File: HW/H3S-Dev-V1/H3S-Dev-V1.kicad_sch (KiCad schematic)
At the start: 20 parts, among them J1 USB_C_Receptacle_USB2.0_16P, J2 Conn_01x02_Socket, J3 Conn_Coaxial, Q1 DMP3099L, U1 Ai-Thinker-Ra-01, U2 LTC4054ES5-4.2, U3 USBLC6-2SC6, U4 ESP32-S3-WROOM-1

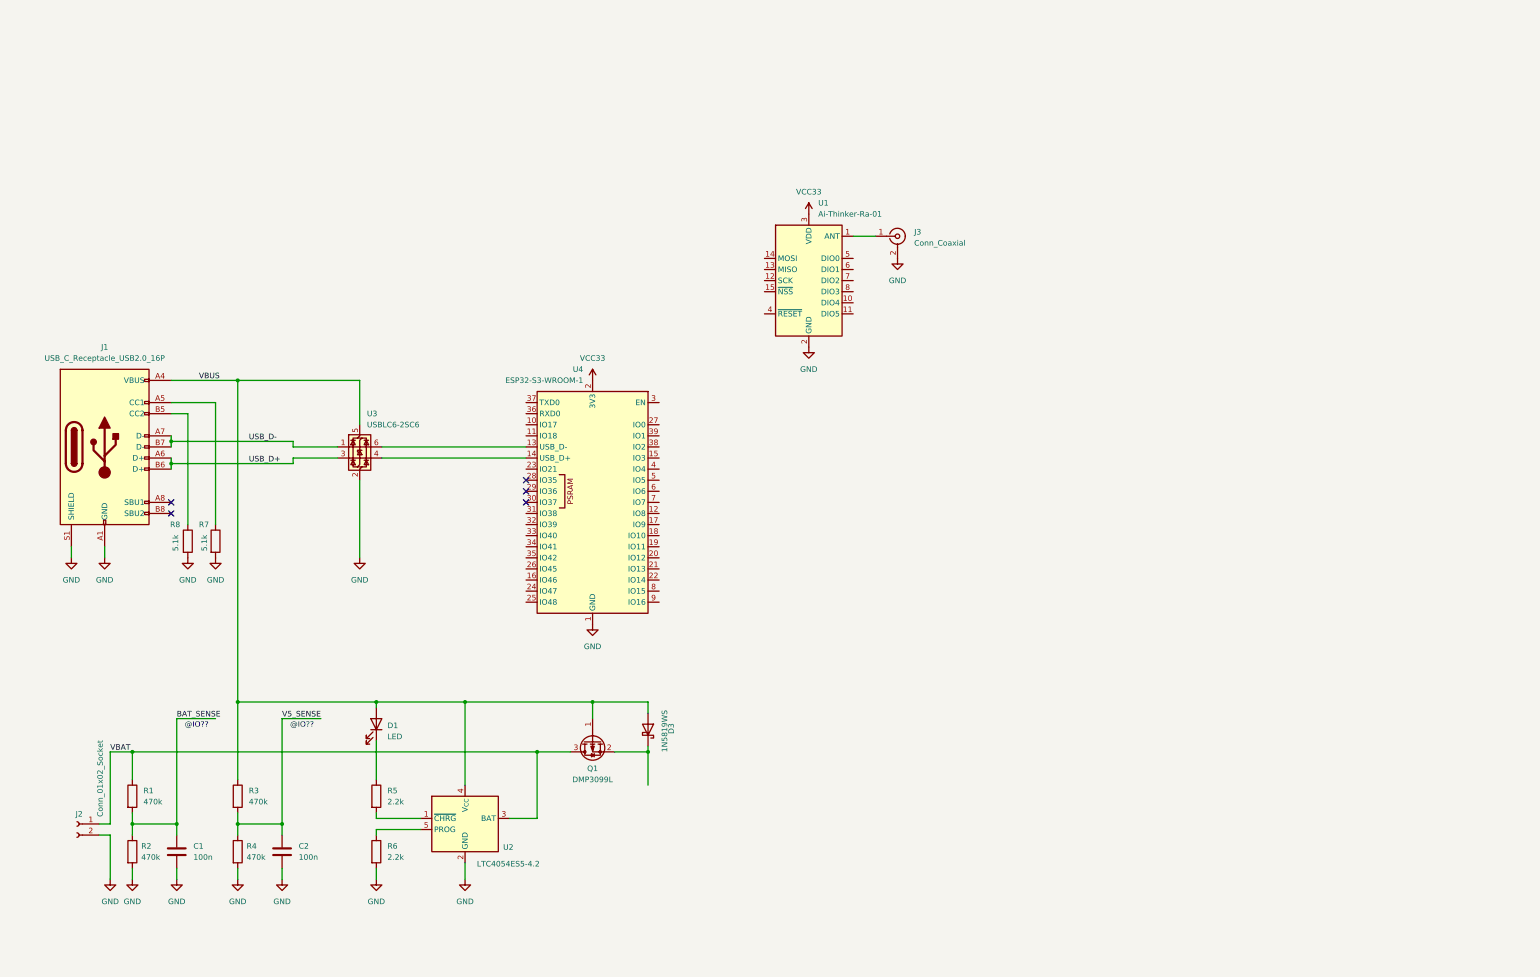
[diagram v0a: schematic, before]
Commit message: Some components arranged
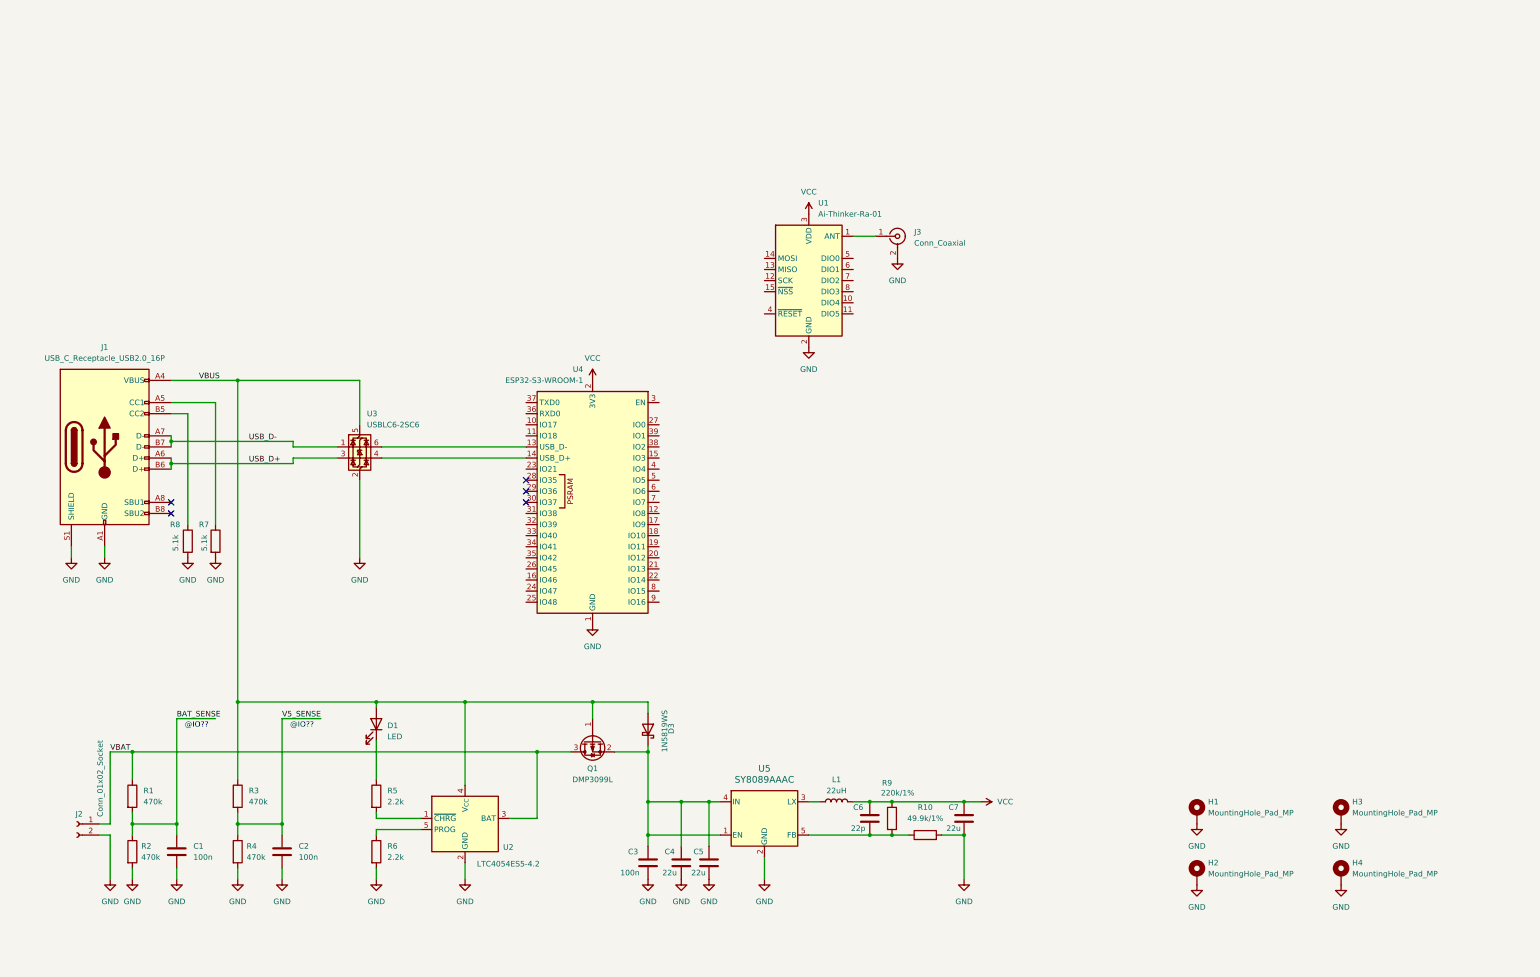
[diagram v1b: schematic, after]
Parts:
- added C3: 100n, Capacitor_SMD:C_0603_1608Metric, symbol Device:C
- added C4, C5, C7: 22u, Capacitor_SMD:C_0603_1608Metric, symbol Device:C
- added C6: 22p, Capacitor_SMD:C_0603_1608Metric, symbol Device:C
- added H1, H2, H3, H4: MountingHole_Pad_MP, MountingHole:MountingHole_2.7mm_M2.5_Pad_Via, symbol Mechanical:MountingHole_Pad_MP
- added L1: 22uH, Inductor_SMD_Wurth:L_Wurth_WE-LQSH-4020, symbol Device:L
- added R10: 49.9k/1%, Resistor_SMD:R_0603_1608Metric, symbol Device:R
- added R9: 220k/1%, Resistor_SMD:R_0603_1608Metric, symbol Device:R
- added U5: SY8089AAAC, Package_TO_SOT_SMD:SOT-23-5, symbol SY8089:SY8089AAAC
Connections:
- net GND: now also C3.2, C4.2, C5.2, C7.2, H1.MP, H2.MP, H3.MP, H4.MP, R10.2, U5.2 (GND)
- net at D3.1 (K), Q1.2 (S): now also C3.1, C4.1, C5.1, U5.1 (EN), U5.4 (IN)
- net VCC33 renamed VCC
- net VCC: now also C6.1, C7.1, L1.2, R9.1
- new net: C6.2, R10.1, R9.2, U5.5 (FB)
- new net: L1.1, U5.3 (LX)

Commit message: dc-dc routing
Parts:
- C4, C5: footprint Capacitor_SMD:C_0603_1608Metric -> Capacitor_SMD:C_0805_2012Metric
- C7: footprint Capacitor_SMD:C_0603_1608Metric -> Capacitor_SMD:C_0805_2012Metric_Pad1.18x1.45mm_HandSolder
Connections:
- net VCC: now also L1.1; no longer L1.2
- net at U5.3 (LX): now also L1.2; no longer L1.1
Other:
- moved on the sheet: L1
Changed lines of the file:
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@@
 	)
 	(junction
-		(at 228.6 208.28)
-		(diameter 0)
-		(color 0 0 0 0)
-	)
-	(junction
 		(at 68.58 125.73)
 		(diameter 0)
@@
 	)
 	(junction
+		(at 228.6 208.28)
+		(diameter 0)
+		(color 0 0 0 0)
+	)
+	(junction
 		(at 228.6 215.9)
 		(diameter 0)
@@
 	(wire
 		(pts
-			(xy 214.63 208.28) (xy 217.17 208.28)
-		)
-		(stroke
-			(width 0)
-			(type default)
-		)
-	)
-	(wire
-		(pts
 			(xy 165.1 185.42) (xy 177.8 185.42)
 		)
@@
 	(wire
 		(pts
+			(xy 224.79 208.28) (xy 228.6 208.28)
+		)
+		(stroke
+			(width 0)
+			(type default)
+		)
+	)
+	(wire
+		(pts
 			(xy 135.89 204.47) (xy 135.89 185.42)
 		)
@@
 	(wire
 		(pts
-			(xy 224.79 208.28) (xy 228.6 208.28)
-		)
-		(stroke
-			(width 0)
-			(type default)
-		)
-	)
-	(wire
-		(pts
 			(xy 177.8 208.28) (xy 177.8 215.9)
 		)
@@
 	(wire
 		(pts
+			(xy 214.63 208.28) (xy 217.17 208.28)
+		)
+		(stroke
+			(width 0)
+			(type default)
+		)
+	)
+	(wire
+		(pts
 			(xy 185.42 208.28) (xy 191.77 208.28)
 		)
@@
 			)
 		)
-		(property "Footprint" "Capacitor_SMD:C_0603_1608Metric"
+		(property "Footprint" "Capacitor_SMD:C_0805_2012Metric_Pad1.18x1.45mm_HandSolder"
 			(at 251.1552 215.9 0)
 			(effects
@@
 	(symbol
 		(lib_id "Device:L")
-		(at 220.98 208.28 90)
+		(at 220.98 208.28 270)
+		(mirror x)
 		(unit 1)
 		(exclude_from_sim no)
@@
 		(on_board yes)
 		(dnp no)
-		(fields_autoplaced yes)
 		(property "Reference" "L1"
 			(at 220.98 203.2 90)
@@
 			)
 		)
-		(property "Footprint" "Capacitor_SMD:C_0603_1608Metric"
+		(property "Footprint" "Capacitor_SMD:C_0805_2012Metric"
 			(at 186.3852 226.06 0)
 			(effects
@@
 			)
 		)
-		(property "Footprint" "Capacitor_SMD:C_0603_1608Metric"
+		(property "Footprint" "Capacitor_SMD:C_0805_2012Metric"
 			(at 192.7352 226.06 0)
 			(effects

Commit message: LoRa, Reset and some more routing
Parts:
- removed H1, H2, H3, H4: MountingHole_Pad_MP, MountingHole:MountingHole_2.7mm_M2.5_Pad_Via, symbol Mechanical:MountingHole_Pad_MP
- added C8: 1u, Capacitor_SMD:C_0603_1608Metric, symbol Device:C
- added C9: 100n, Capacitor_SMD:C_0603_1608Metric, symbol Device:C
- added H1, H2, H3, H4: MountingHole, MountingHole:MountingHole_2.2mm_M2, symbol Mechanical:MountingHole
- added R11: 10k, Resistor_SMD:R_0603_1608Metric, symbol Device:R
- added SW1: SW_Push, Button_Switch_SMD:SW_Tactile_SPST_NO_Straight_CK_PTS636Sx25SMTRLFS, symbol Switch:SW_Push
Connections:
- net GND: now also C8.2, C9.2, SW1.2
- net VCC: now also R11.1
- net DIO4: now reaches U1.10 (DIO4)
- net DIO5: now reaches U1.11 (DIO5)
- net SCK: now reaches U1.12 (SCK)
- net SCK: now also U4.5 (IO5)
- net MISO: now reaches U1.13 (MISO)
- net MISO: now also U4.15 (IO3)
- net MOSI: now reaches U1.14 (MOSI)
- net MOSI: now also U4.6 (IO6)
- net ~{SS}: now reaches U1.15 (~{NSS})
- net ~{SS}: now also U4.7 (IO7)
- net ~{LoRa_RST}: now reaches U1.4 (~{RESET})
- net ~{LoRa_RST}: now also U4.12 (IO8)
- net DIO0: now reaches U1.5 (DIO0)
- net DIO0: now also U4.8 (IO15)
- net DIO1: now reaches U1.6 (DIO1)
- net DIO1: now also U4.9 (IO16)
- net DIO2: now reaches U1.7 (DIO2)
- net DIO2: now also U4.10 (IO17)
- net DIO3: now reaches U1.8 (DIO3)
- net ~{ESP_EN}: now reaches U4.3 (EN)
- net ~{ESP_EN}: now also C8.1, C9.1, R11.2, SW1.1
- no-connect marks 5 -> 8
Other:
- note added: "strapping!"
- moved on the sheet: J3, U1

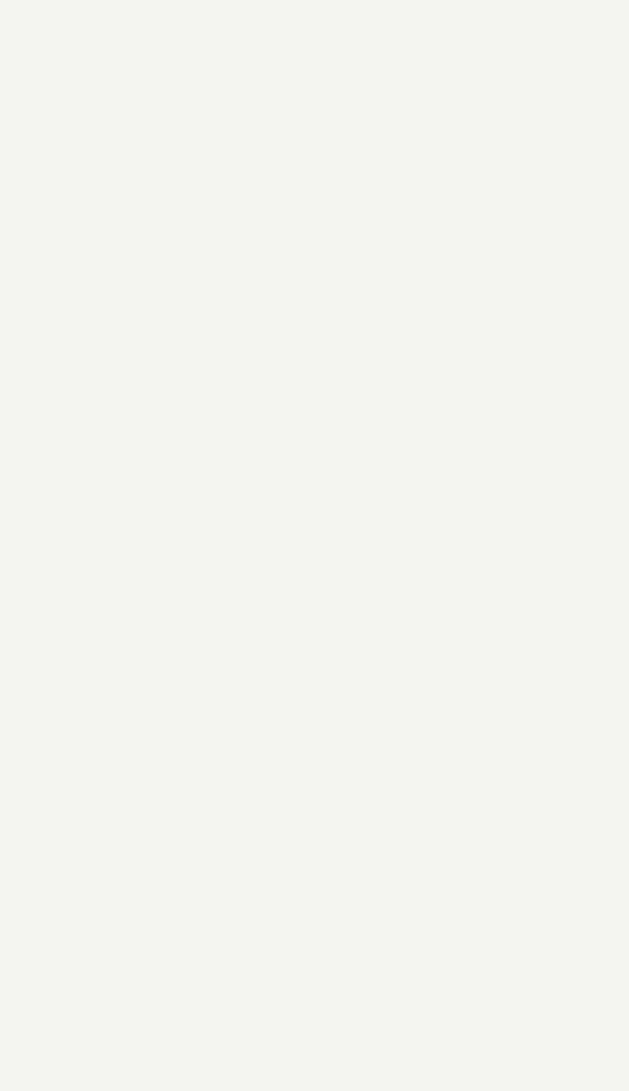
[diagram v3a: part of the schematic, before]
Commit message: GNSS Module added
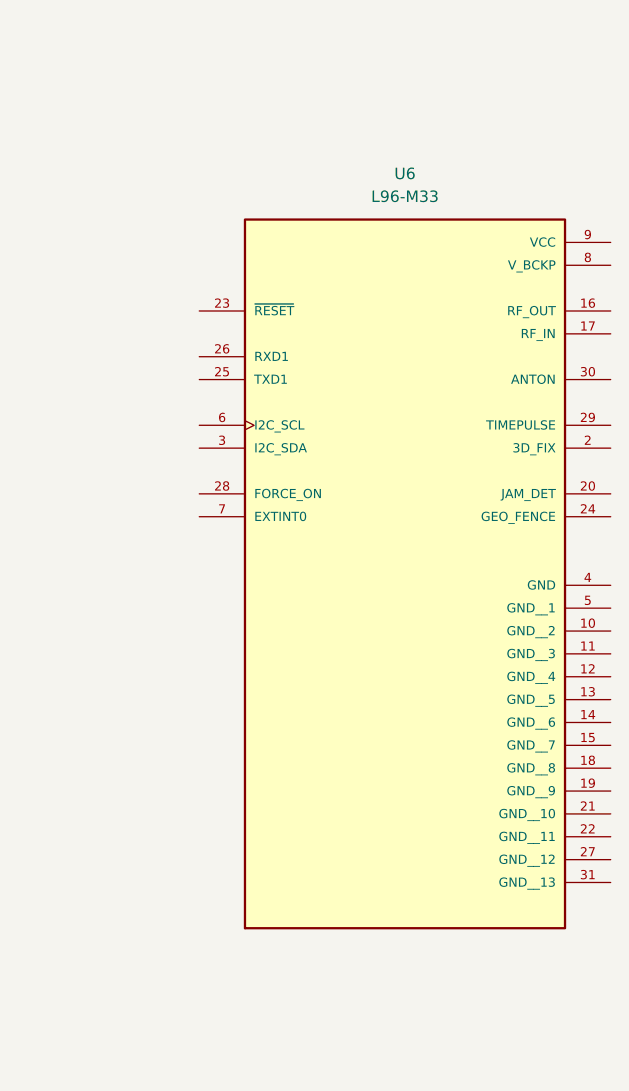
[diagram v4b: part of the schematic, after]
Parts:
- added U6: L96-M33, L96_M33:XCVR_L96-M33, symbol L96-M33:L96-M33
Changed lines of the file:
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@@
+	)
+	(symbol
+		(lib_id "L96-M33:L96-M33")
+		(at 344.17 119.38 0)
+		(unit 1)
+		(exclude_from_sim no)
+		(in_bom yes)
+		(on_board yes)
+		(dnp no)
+		(fields_autoplaced yes)
+		(property "Reference" "U6"
+			(at 344.17 91.44 0)
+			(effects
+				(font
+					(size 1.27 1.27)
+				)
+			)
+		)
+		(property "Value" "L96-M33"
+			(at 344.17 93.98 0)
+			(effects
+				(font
+					(size 1.27 1.27)
+				)
+			)
+		)
+		(property "Footprint" "L96_M33:XCVR_L96-M33"
+			(at 344.17 119.38 0)
+			(effects
+				(font
+					(size 1.27 1.27)
+				)
+				(justify bottom)
+				(hide yes)
+			)
+		)
+		(property "Datasheet" ""
+			(at 344.17 119.38 0)
+			(effects
+				(font
+					(size 1.27 1.27)
+				)
+				(hide yes)
+			)
+		)
+		(property "Description" ""
+			(at 344.17 119.38 0)
+			(effects
+				(font
+					(size 1.27 1.27)
+				)
+				(hide yes)
+			)
+		)
+		(property "MF" "Quectel Wireless Solutions Co., Ltd"
+			(at 344.17 119.38 0)
+			(effects
+				(font
+					(size 1.27 1.27)
+				)
+				(justify bottom)
+				(hide yes)
+			)
+		)
+		(property "DESCRIPTION" "L96 is a concurrent multi-GNSS receiver module with embedded chip antenna. With 33 tracking channels, 99 acquisition channels and 210 PRN channels, L96 supports concurrent reception of up to three GNSS systems _GPS+GLONASS+Galileo_"
+			(at 344.17 119.38 0)
+			(effects
+				(font
+					(size 1.27 1.27)
+				)
+				(justify bottom)
+				(hide yes)
+			)
+		)
+		(property "PACKAGE" "SOIC-8 Quectel Wireless Solutions Co., Ltd"
+			(at 344.17 119.38 0)
+			(effects
+				(font
+					(size 1.27 1.27)
+				)
+				(justify bottom)
+				(hide yes)
+			)
+		)
+		(property "PRICE" "None"
+			(at 344.17 119.38 0)
+			(effects
+				(font
+					(size 1.27 1.27)
+				)
+				(justify bottom)
+				(hide yes)
+			)
+		)
+		(property "MP" "L96"
+			(at 344.17 119.38 0)
+			(effects
+				(font
+					(size 1.27 1.27)
+				)
+				(justify bottom)
+				(hide yes)
+			)
+		)
+		(property "AVAILABILITY" "Unavailable"
+			(at 344.17 119.38 0)
+			(effects
+				(font
+					(size 1.27 1.27)
+				)
+				(justify bottom)
+				(hide yes)
+			)
+		)
+		(pin "31"
+		)
+		(pin "8"
+		)
+		(pin "4"
+		)
+		(pin "18"
+		)
+		(pin "15"
+		)
+		(pin "10"
+		)
+		(pin "17"
+		)
+		(pin "20"
+		)
+		(pin "16"
+		)
+		(pin "9"
+		)
+		(pin "29"
+		)
+		(pin "24"
+		)
+		(pin "27"
+		)
+		(pin "14"
+		)
+		(pin "12"
+		)
+		(pin "11"
+		)
+		(pin "22"
+		)
+		(pin "13"
+		)
+		(pin "30"
+		)
+		(pin "2"
+		)
+		(pin "7"
+		)
+		(pin "28"
+		)
+		(pin "3"
+		)
+		(pin "6"
+		)
+		(pin "25"
+		)
+		(pin "26"
+		)
+		(pin "23"
+		)
+		(pin "21"
+		)
+		(pin "5"
+		)
+		(pin "19"
+		)
+		(instances
+			(project ""
+				(path "/bea38324-05bc-47f3-9040-a69798280d79"
+					(reference "U6")
+					(unit 1)
+				)
+			)
+		)
 	)
 	(symbol

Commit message: Some progress...
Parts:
- added J4, J5: Conn_01x04, Connector:NS-Tech_Grove_1x04_P2mm_Vertical, symbol Connector_Generic:Conn_01x04
- added R12, R13, R14, R15: 10k, Resistor_SMD:R_0603_1608Metric, symbol Device:R
- added R16: 0, Resistor_SMD:R_0603_1608Metric, symbol Device:R
- U6: footprint L96_M33:XCVR_L96-M33 -> XCVR_L96-M33; DESCRIPTION L96 is a concurrent multi-GNSS receiver module with embedde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 -> (none)
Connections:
- net GND: now also U6.10 (GND__2), U6.11 (GND__3), U6.12 (GND__4), U6.13 (GND__5), U6.14 (GND__6), U6.15 (GND__7), U6.18 (GND__8), U6.19 (GND__9), U6.21 (GND__10), U6.22 (GND__11), U6.27 (GND__12), U6.30 (ANTON), U6.31 (GND__13), U6.4 (GND), U6.5 (GND__1), J4.4 (Pin_4), J5.4 (Pin_4)
- net VCC: now also U6.8 (V_BCKP), U6.9 (VCC), J4.3 (Pin_3), J5.3 (Pin_3), R12.1, R13.1, R14.1, R15.1, R16.1
- net SCL: now reaches U4.38 (IO2)
- net SCL: now also J4.1 (Pin_1), J5.1 (Pin_1), R12.2, R14.2
- net SDA: now reaches U4.39 (IO1)
- net SDA: now also J4.2 (Pin_2), J5.2 (Pin_2), R13.2, R15.2
- net at U6.16 (RF_OUT): now also U6.17 (RF_IN)
- new net: R16.2, U6.1 (VCC_IO)
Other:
- moved on the sheet: H1, H2, H3
